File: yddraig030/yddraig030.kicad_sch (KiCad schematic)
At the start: 0 parts

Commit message: More work on the 030 board
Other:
- added sheet Serial Ports (serial.kicad_sch)

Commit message: Updated 030 design files
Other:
- removed sheet Expansion Bus
- removed sheet IDE Interface
- removed sheet Serial Ports
- added sheet DRAM (DRAM.kicad_sch)
- added sheet Decode and Logic (Decode.kicad_sch)
- added sheet Ethernet (Ethernet.kicad_sch)
- added sheet Expansion Slots (Expansion.kicad_sch)
- added sheet IDE (IDE Interface.kicad_sch)
- added sheet Interrupts (interrupts.kicad_sch)
- added sheet Parallel Port (parallel.kicad_sch)
- added sheet Reset and LEDs (Reset.kicad_sch)
- added sheet Serial (Serial.kicad_sch)
- sheet CPU and FPU ports: added A[0..31], D[0..31], FC[0..2], R~{W}, SIZ0, SIZ1, ~{AS}, ~{BERR}, ~{CBREQ}, ~{CDIS}, ~{CS_FPU}, ~{DSACK0}, ~{DSACK1}, ~{DS}, ~{FPUSENSE}, ~{HALT}, ~{IPL[0..2]}, ~{MMUDIS}, ~{RESET}, ~{STERM}; removed none
- sheet Keyboard ports: added A[0..31], D[0..31], RD/~{WR}, ~{CS_KBD}, ~{INT_KBD}, ~{INT_MOUSE}, ~{RD}/WR, ~{RESET}; removed none
- sheet Power: file Powersch.kicad_sch -> Power.kicad_sch
- sheet ROM and SRAM: file ROM_SRAM.kicad_sch -> ROMRAM.kicad_sch
- sheet ROM and SRAM ports: added A[0..31], D[0..31], RD/~{WR}, ~{CS_ROM}, ~{CS_SRAM}, ~{LDS}, ~{RD}/WR, ~{UDS}; removed none
- sheet Real Time Clock ports: added A[0..31], D[0..31], RD/~{WR}, ~{CS_RTC}, ~{RD}/WR, ~{RESET}; removed none
- note added: "Notes: To be fixed... DSACKx from decode needs to be open collector Pullups on CPU pins and DSACK Check signals needed from CPU CPU clock and 10Mhz clock needed"
- company: (none) -> Stephen Moody
- title: (none) -> Y Ddraig Fawr

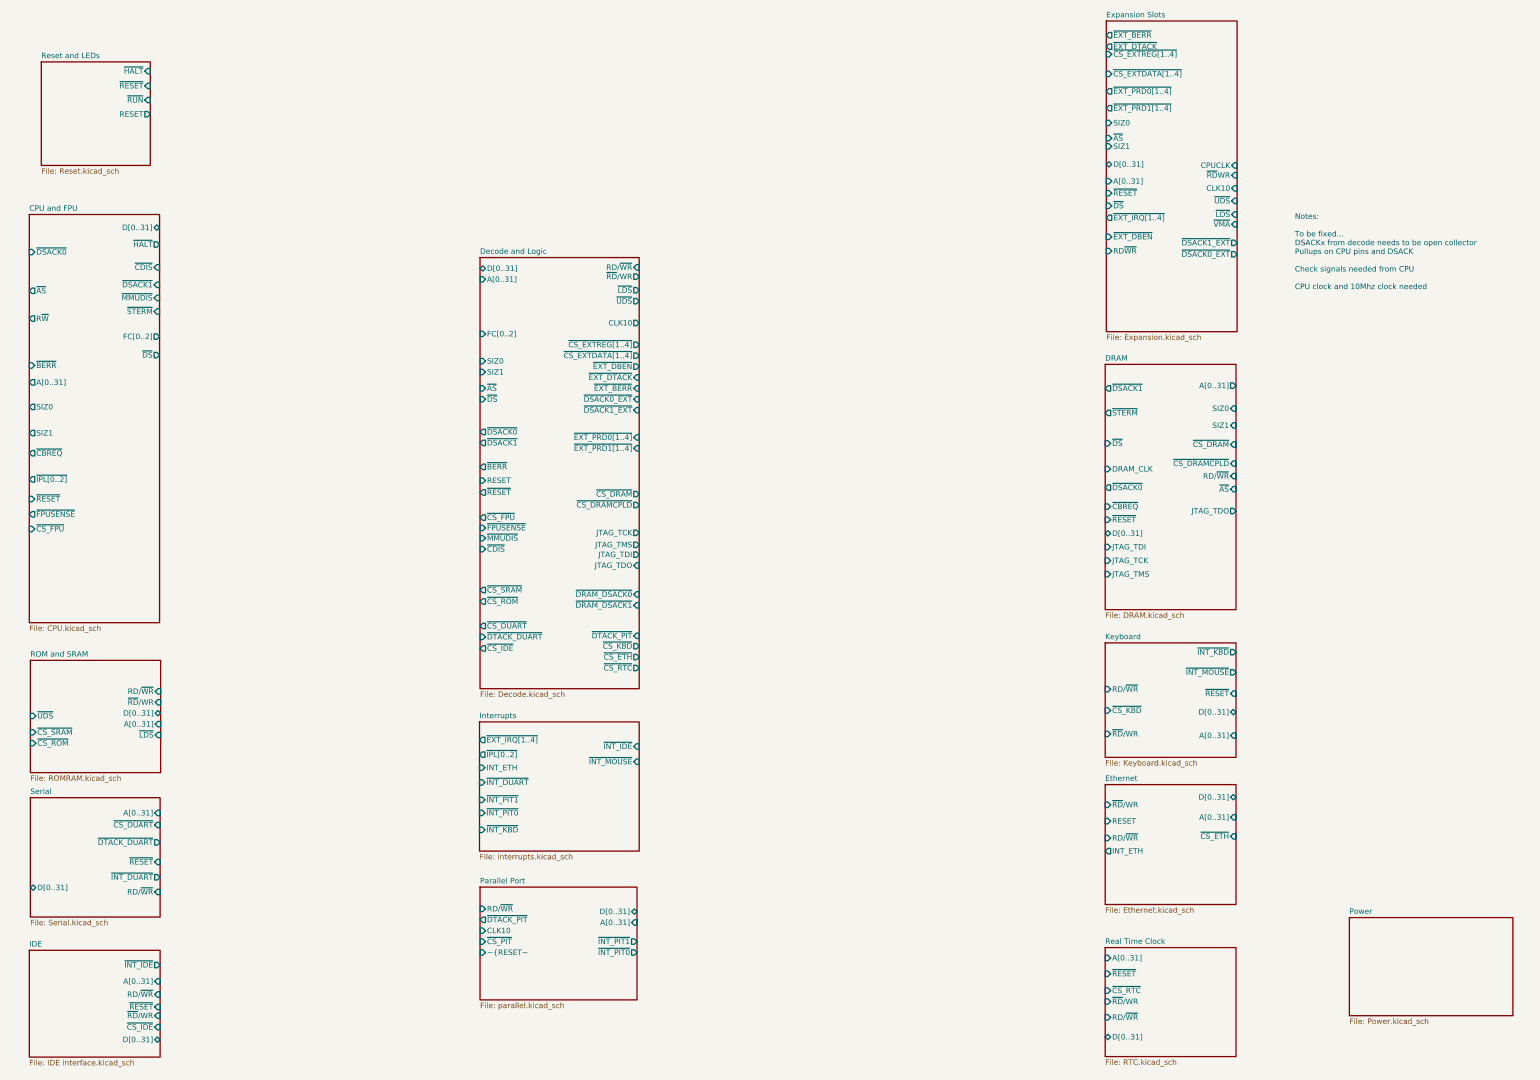
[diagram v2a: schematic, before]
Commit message: More changes to the 030 board
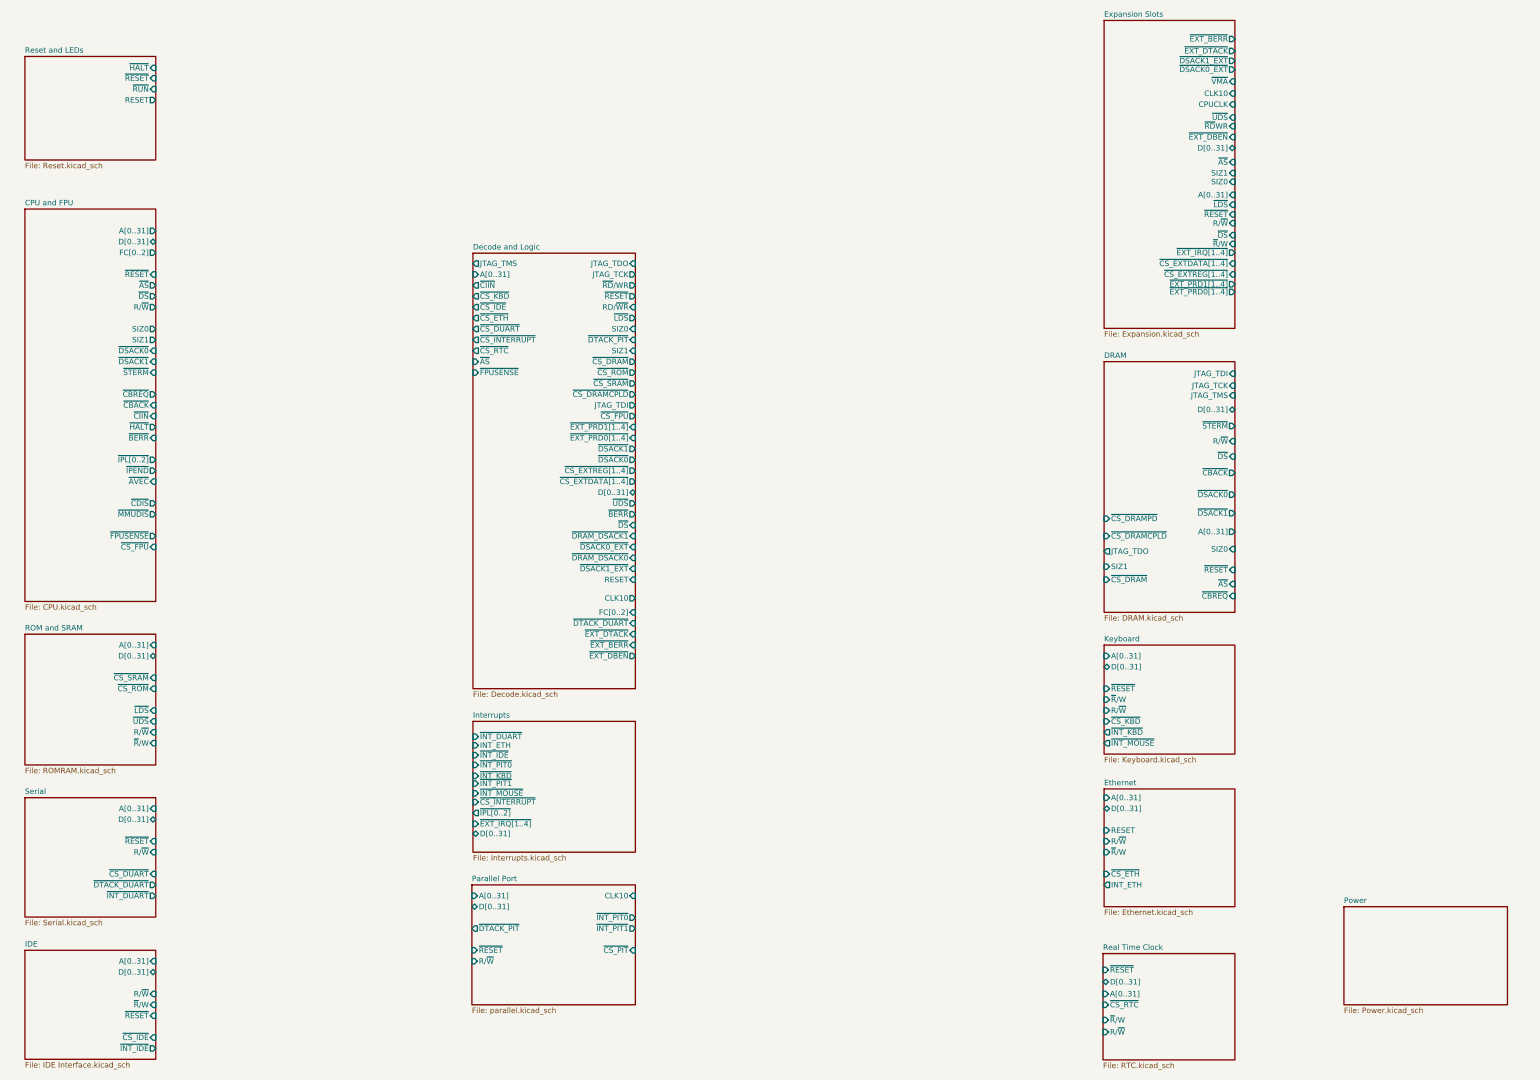
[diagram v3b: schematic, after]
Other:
- sheet CPU and FPU ports: added R/~{W}, ~{AVEC}, ~{CBACK}, ~{CIIN}, ~{IPEND}; removed R~{W}
- sheet DRAM ports: added R/~{W}, ~{CBACK}, ~{CS_DRAMPD}; removed DRAM_CLK, RD/~{WR}
- sheet Decode and Logic ports: added ~{CIIN}, ~{CS_INTERRUPT}; removed ~{CDIS}, ~{MMUDIS}
- sheet Ethernet ports: added R/~{W}, ~{R}/W; removed RD/~{WR}, ~{RD}/WR
- sheet Expansion Slots ports: added R/~{W}, ~{R}/W; removed RD~{WR}
- sheet IDE ports: added R/~{W}, ~{R}/W; removed RD/~{WR}, ~{RD}/WR
- sheet Interrupts ports: added D[0..31], ~{CS_INTERRUPT}; removed none
- sheet Keyboard ports: added R/~{W}, ~{R}/W; removed RD/~{WR}, ~{RD}/WR
- sheet Parallel Port ports: added R/~{W}, ~{RESET}; removed RD/~{WR}, ~{RESET~
- sheet ROM and SRAM ports: added R/~{W}, ~{R}/W; removed RD/~{WR}, ~{RD}/WR
- sheet Real Time Clock ports: added R/~{W}, ~{R}/W; removed RD/~{WR}, ~{RD}/WR
- sheet Serial ports: added R/~{W}; removed RD/~{WR}
- note removed: "Notes: To be fixed... DSACKx from decode needs to be open collector Pullups on CPU pins and DSACK Check signals needed from CPU CPU clock and 10Mhz clock needed"

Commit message: ddraig030 schematic done
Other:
- sheet CPU and FPU ports: added CPU_CLK; removed none
- sheet Decode and Logic ports: added R/~{W}, ~{AVEC}, ~{CDIS}, ~{CS_DRAMPD}, ~{CS_PIT}, ~{IPEND}, ~{MMUDIS}, ~{R}/W, ~{VMA}; removed RD/~{WR}, ~{RD}/WR
- sheet Expansion Slots ports: added none; removed ~{RD}WR

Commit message: Small changes to 030 design
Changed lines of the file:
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@@
     (stroke (width 0) (type default) (color 0 0 0 0))
   )
-  (bus (pts (xy 175.514 185.42) (xy 213.36 185.42))
+  (bus (pts (xy 175.26 185.42) (xy 213.36 185.42))
     (stroke (width 0) (type default) (color 0 0 0 0))
   )
@@
     )
     (path "/00000000-0000-0000-0000-000060eb395d/00000000-0000-0000-0000-000060eb72be"
-      (reference "U301") (unit 1) (value "MC68030") (footprint "Ddraig:QFP-128_28x28_Pitch0.8mm")
+      (reference "U301") (unit 1) (value "MC68030") (footprint "Ddraig:MC68030RC")
     )
     (path "/00000000-0000-0000-0000-000060eb395d/00000000-0000-0000-0000-000060fcab24"
